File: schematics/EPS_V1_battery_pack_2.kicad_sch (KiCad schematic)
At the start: 31 parts, among them U8 MP2672AGD-0000-Z, U9 MAX17205G+

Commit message: Fix NC pins, add 2 test points & silkscreen labels
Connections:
- net GND: now also U8.14 (SCL), U8.15 (SDA), U9.10 (AIN2), U9.9 (AIN1)
- no-connect marks 6 -> 2
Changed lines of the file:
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@@
 	)
 	(junction
+		(at 104.14 91.44)
+		(diameter 0)
+		(color 0 0 0 0)
+	)
+	(junction
+		(at 104.14 88.9)
+		(diameter 0)
+		(color 0 0 0 0)
+	)
+	(junction
 		(at 58.42 67.31)
 		(diameter 0)
@@
 	)
 	(junction
+		(at 229.87 87.63)
+		(diameter 0)
+		(color 0 0 0 0)
+	)
+	(junction
 		(at 73.66 118.11)
 		(diameter 0)
@@
 	)
 	(no_connect
-		(at 104.14 88.9)
-	)
-	(no_connect
-		(at 229.87 90.17)
-	)
-	(no_connect
 		(at 229.87 77.47)
 	)
-	(no_connect
-		(at 104.14 86.36)
-	)
-	(no_connect
-		(at 229.87 87.63)
-	)
 	(wire
 		(pts
@@
 	(wire
 		(pts
+			(xy 229.87 95.25) (xy 229.87 92.71)
+		)
+		(stroke
+			(width 0)
+			(type default)
+		)
+	)
+	(wire
+		(pts
+			(xy 229.87 87.63) (xy 233.68 87.63)
+		)
+		(stroke
+			(width 0)
+			(type default)
+		)
+	)
+	(wire
+		(pts
 			(xy 45.72 106.68) (xy 41.91 106.68)
 		)
@@
 	(wire
 		(pts
+			(xy 104.14 86.36) (xy 104.14 88.9)
+		)
+		(stroke
+			(width 0)
+			(type default)
+		)
+	)
+	(wire
+		(pts
 			(xy 29.21 67.31) (xy 38.1 67.31)
 		)
@@
 	(wire
 		(pts
-			(xy 58.42 83.82) (xy 63.5 83.82)
+			(xy 229.87 95.25) (xy 232.41 95.25)
 		)
 		(stroke
@@
 	(wire
 		(pts
-			(xy 179.07 110.49) (xy 179.07 80.01)
+			(xy 58.42 83.82) (xy 63.5 83.82)
 		)
 		(stroke
@@
 	(wire
 		(pts
-			(xy 229.87 92.71) (xy 231.14 92.71)
+			(xy 179.07 110.49) (xy 179.07 80.01)
 		)
 		(stroke
@@
 	(wire
 		(pts
+			(xy 104.14 88.9) (xy 104.14 91.44)
+		)
+		(stroke
+			(width 0)
+			(type default)
+		)
+	)
+	(wire
+		(pts
+			(xy 229.87 87.63) (xy 229.87 90.17)
+		)
+		(stroke
+			(width 0)
+			(type default)
+		)
+	)
+	(wire
+		(pts
 			(xy 181.61 101.6) (xy 196.85 101.6)
 		)
@@
 	(global_label "ALRT"
 		(shape output)
-		(at 231.14 92.71 0)
+		(at 232.41 95.25 0)
 		(fields_autoplaced yes)
 		(effects
@@
 		)
 		(property "Intersheetrefs" "${INTERSHEET_REFS}"
-			(at 238.4795 92.71 0)
+			(at 239.7495 95.25 0)
 			(hide yes)
 			(show_name no)
@@
 					(unit 1)
 				)
+			)
+		)
+	)
+	(symbol
+		(lib_id "power:GND")
+		(at 233.68 87.63 0)
+		(unit 1)
+		(body_style 1)
+		(exclude_from_sim no)
+		(in_bom yes)
+		(on_board yes)
+		(in_pos_files yes)
+		(dnp no)
+		(property "Reference" "#PWR0131"
+			(at 233.68 93.98 0)
+			(hide yes)
+			(show_name no)
+			(do_not_autoplace no)
+			(effects
+				(font
+					(size 1.27 1.27)
+				)
+			)
+		)
+		(property "Value" "GND"
+			(at 233.68 91.694 0)
+			(show_name no)
+			(do_not_autoplace no)
+			(effects
+				(font
+					(size 1.27 1.27)
+				)
+			)
+		)
+		(property "Footprint" ""
+			(at 233.68 87.63 0)
+			(hide yes)
+			(show_name no)
+			(do_not_autoplace no)
+			(effects
+				(font
+					(size 1.27 1.27)
+				)
+			)
+		)
+		(property "Datasheet" ""
+			(at 233.68 87.63 0)
+			(hide yes)
+			(show_name no)
+			(do_not_autoplace no)
+			(effects
+				(font
+					(size 1.27 1.27)
+				)
+			)
+		)
+		(property "Description" "Power symbol creates a global label with name \"GND\" , ground"
+			(at 233.68 87.63 0)
+			(hide yes)
+			(show_name no)
+			(do_not_autoplace no)
+			(effects
+				(font
+					(size 1.27 1.27)
+				)
+			)
+		)
+		(pin "1"
+		)
+		(instances
+			(project "EPS_V1"
+				(path "/85157432-5d03-48fa-ab40-27ed3d133f47/1a447d2c-bf0d-40e4-b56c-2660ef69d96a"
+					(reference "#PWR0131")
+					(unit 1)
+				)

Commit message: Fix silkscreen; Fix component value style
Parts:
- C_BATT4, C_BST2: value 0.1u -> 100n
- C_REG4, C_REG5: value 0.47u -> 470n
- R_BATT2, R_MID2: value 50 -> 50R
- R_SCL2, R_SDA2: value 150 -> 150R
- R_SENSE2: value 0.01 -> 10m
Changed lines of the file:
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@@
 			)
 		)
-		(property "Value" "150"
+		(property "Value" "150R"
 			(at 247.904 89.916 90)
 			(show_name no)
@@
 			)
 		)
-		(property "Value" "0.47u"
+		(property "Value" "470n"
 			(at 172.212 100.33 0)
 			(show_name no)
@@
 			)
 		)
-		(property "Value" "0.1u"
+		(property "Value" "100n"
 			(at 55.118 78.74 0)
 			(show_name no)
@@
 			)
 		)
-		(property "Value" "50"
+		(property "Value" "50R"
 			(at 61.722 101.6 0)
 			(show_name no)
@@
 		(dnp no)
 		(property "Reference" "D_SCL2"
-			(at 237.49 87.63 90)
+			(at 236.22 87.63 90)
 			(show_name no)
 			(do_not_autoplace no)
@@
 			)
 		)
-		(property "Value" "0.1u"
+		(property "Value" "100n"
 			(at 167.132 87.63 0)
 			(show_name no)
@@
 			)
 		)
-		(property "Value" "0.47u"
+		(property "Value" "470n"
 			(at 182.118 115.57 0)
 			(show_name no)
@@
 			)
 		)
-		(property "Value" "50"
+		(property "Value" "50R"
 			(at 165.354 80.264 90)
 			(show_name no)
@@
 			)
 		)
-		(property "Value" "0.01"
+		(property "Value" "10m"
 			(at 201.676 106.934 90)
 			(show_name no)
@@
 			)
 		)
-		(property "Value" "150"
+		(property "Value" "150R"
 			(at 263.144 77.724 90)
 			(show_name no)

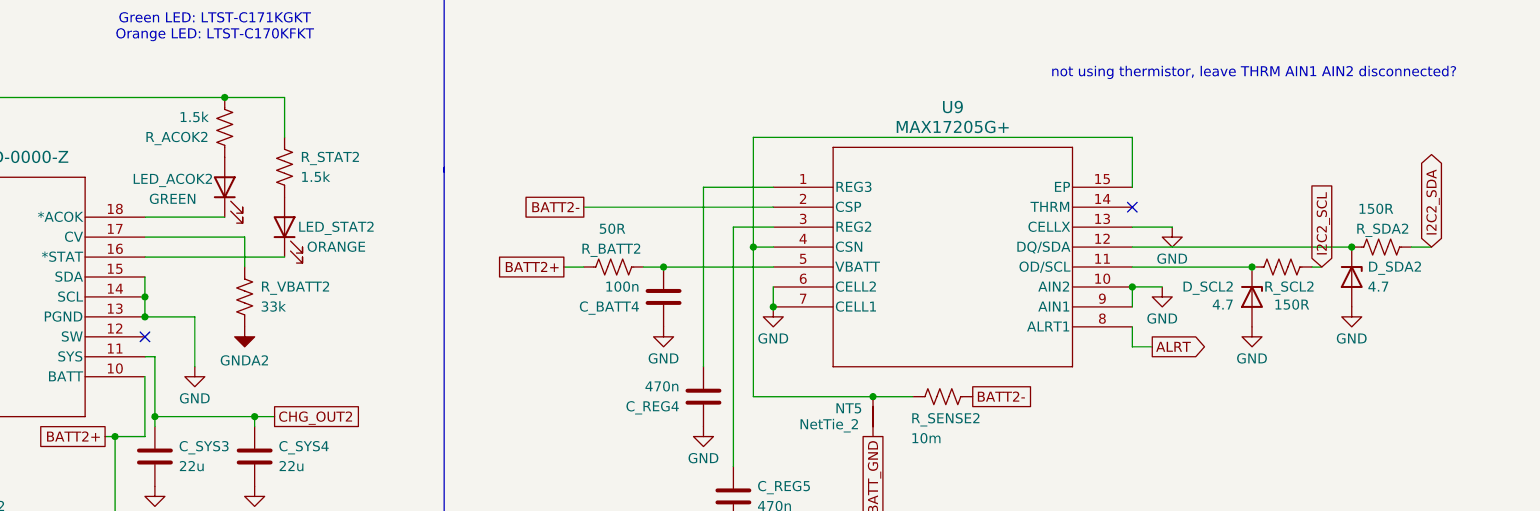
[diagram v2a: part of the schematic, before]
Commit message: Add chargers to I2C, chg_in for ADC
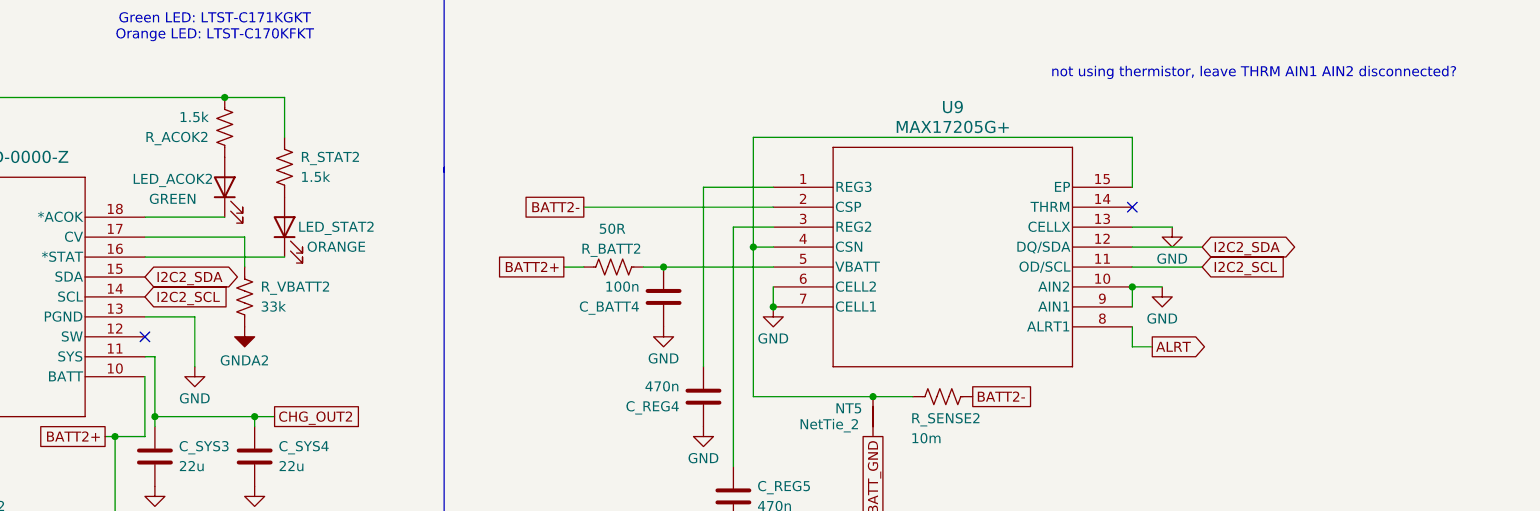
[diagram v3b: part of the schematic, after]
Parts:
- removed D_SCL2, D_SDA2: 4.7, Diode_SMD:D_0603_1608Metric, symbol Device:D_Zener
- removed R_SCL2, R_SDA2: 150R, Resistor_SMD:R_0603_1608Metric, symbol Device:R_US
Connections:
- net GND: no longer U8.14 (SCL), U8.15 (SDA)
- net I2C2_SCL: now also U8.14 (SCL), U9.11 (OD/SCL)
- net I2C2_SDA: now also U8.15 (SDA), U9.12 (DQ/SDA)

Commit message: Fix standalone to host control mode
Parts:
- removed R_VBATT2: 33k, Resistor_SMD:R_0603_1608Metric, symbol Device:R_US
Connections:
- net at C_VCC2.2, R_ACOK2.2, R_STAT2.1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: now also U8.17 (CV)
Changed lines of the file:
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@@
 	)
 	(junction
+		(at 105.41 63.5)
+		(diameter 0)
+		(color 0 0 0 0)
+	)
+	(junction
 		(at 58.42 67.31)
 		(diameter 0)
@@
 	(wire
 		(pts
+			(xy 105.41 63.5) (xy 48.26 63.5)
+		)
+		(stroke
+			(width 0)
+			(type default)
+		)
+	)
+	(wire
+		(pts
 			(xy 100.33 106.68) (xy 104.14 106.68)
 		)
@@
 	(wire
 		(pts
+			(xy 104.14 81.28) (xy 105.41 81.28)
+		)
+		(stroke
+			(width 0)
+			(type default)
+		)
+	)
+	(wire
+		(pts
 			(xy 27.94 67.31) (xy 29.21 67.31)
 		)
@@
 	(wire
 		(pts
+			(xy 105.41 81.28) (xy 105.41 63.5)
+		)
+		(stroke
+			(width 0)
+			(type default)
+		)
+	)
+	(wire
+		(pts
 			(xy 118.11 104.14) (xy 118.11 105.41)
 		)
@@
 		)
 	)
-	(wire
-		(pts
-			(xy 104.14 81.28) (xy 116.84 81.28)
-		)
-		(stroke
-			(width 0)
-			(type default)
-		)
-	)
 	(polyline
 		(pts
@@
 	(wire
 		(pts
-			(xy 114.3 63.5) (xy 48.26 63.5)
-		)
-		(stroke
-			(width 0)
-			(type default)
-		)
-	)
-	(wire
-		(pts
-			(xy 116.84 81.28) (xy 116.84 85.09)
+			(xy 114.3 63.5) (xy 105.41 63.5)
 		)
 		(stroke
@@
 	)
 	(symbol
-		(lib_id "sym_lib:GNDA2")
-		(at 116.84 92.71 0)
-		(unit 1)
-		(body_style 1)
-		(exclude_from_sim no)
-		(in_bom no)
-		(on_board no)
-		(in_pos_files yes)
-		(dnp no)
-		(property "Reference" "#PWR0127"
-			(at 116.84 92.71 0)
-			(hide yes)
-			(show_name no)
-			(do_not_autoplace no)
-			(effects
-				(font
-					(size 1.27 1.27)
-				)
-			)
-		)
-		(property "Value" "GNDA2"
-			(at 116.84 97.028 0)
-			(show_name no)
-			(do_not_autoplace no)
-			(effects
-				(font
-					(size 1.27 1.27)
-				)
-			)
-		)
-		(property "Footprint" ""
-			(at 116.84 92.71 0)
-			(hide yes)
-			(show_name no)
-			(do_not_autoplace no)
-			(effects
-				(font
-					(size 1.27 1.27)
-				)
-			)
-		)
-		(property "Datasheet" ""
-			(at 116.84 92.71 0)
-			(hide yes)
-			(show_name no)
-			(do_not_autoplace no)
-			(effects
-				(font
-					(size 1.27 1.27)
-				)
-			)
-		)
-		(property "Description" ""
-			(at 116.84 92.71 0)
-			(hide yes)
-			(show_name no)
-			(do_not_autoplace no)
-			(effects
-				(font
-					(size 1.27 1.27)
-				)
-			)
-		)
-		(pin "1"
-		)
-		(instances
-			(project "EPS_V1"
-				(path "/85157432-5d03-48fa-ab40-27ed3d133f47/1a447d2c-bf0d-40e4-b56c-2660ef69d96a"
-					(reference "#PWR0127")
-					(unit 1)
-				)
-			)
-		)
-	)
-	(symbol
 		(lib_id "power:GND")
 		(at 105.41 113.03 0)
@@
 					(unit 1)
 				)
-			)
-		)
-	)
-	(symbol
-		(lib_id "Device:R_US")
-		(at 116.84 88.9 0)
-		(unit 1)
-		(body_style 1)
-		(exclude_from_sim no)
-		(in_bom yes)
-		(on_board yes)
-		(in_pos_files yes)
-		(dnp no)
-		(property "Reference" "R_VBATT2"
-			(at 118.872 87.63 0)
-			(show_name no)
-			(do_not_autoplace no)
-			(effects
-				(font
-					(size 1.27 1.27)
-				)
-				(justify left)
-			)
-		)
-		(property "Value" "33k"
-			(at 118.872 90.17 0)
-			(show_name no)
-			(do_not_autoplace no)
-			(effects
-				(font
-					(size 1.27 1.27)
-				)
-				(justify left)
-			)
-		)
-		(property "Footprint" "Resistor_SMD:R_0603_1608Metric"
-			(at 117.856 89.154 90)
-			(hide yes)
-			(show_name no)
-			(do_not_autoplace no)
-			(effects
-				(font
-					(size 1.27 1.27)
-				)
-			)
-		)
-		(property "Datasheet" ""
-			(at 116.84 88.9 0)
-			(hide yes)
-			(show_name no)
-			(do_not_autoplace no)
-			(effects
-				(font
-					(size 1.27 1.27)
-				)
-			)
-		)
-		(property "Description" "Resistor, US symbol"
-			(at 116.84 88.9 0)
-			(hide yes)
-			(show_name no)
-			(do_not_autoplace no)
-			(effects
-				(font
-					(size 1.27 1.27)
-				)
-			)
-		)
-		(pin "2"
-		)
-		(pin "1"
-		)
-		(instances
-			(project "EPS_V1"
-				(path "/85157432-5d03-48fa-ab40-27ed3d133f47/1a447d2c-bf0d-40e4-b56c-2660ef69d96a"
-					(reference "R_VBATT2")
-					(unit 1)
-				)

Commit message: fix U6 EN pin, add ALRT pullup R, update 3dmodels, regen step
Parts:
- R_ISET2: value 6k -> 24k
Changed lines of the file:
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@@
 			)
 		)
-		(property "Value" "6k"
+		(property "Value" "24k"
 			(at 48.768 129.54 0)
 			(show_name no)
